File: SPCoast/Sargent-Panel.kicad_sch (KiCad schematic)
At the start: 9 parts, among them U1 0x2C

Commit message: refactor(kicad): Name on every device, office unit and encoding; Kind on the JMRI drivers; Driver-JMRI-Light
The owner's rulings of 2026-10-24 on the review of ADR 0008 rev 4: Name = ${Value}
is the identity key everywhere, devices included; the OfficeUnit's Columns is
derived and struck; a JMRI driver carries no address and is keyed by its object
class and the device it serves, the class carried by Kind (TURNOUT, SENSOR,
SIGNALMAST, LIGHT); Driver-JMRI-Light (ADR 0005 §8: ON, INTENSITY) for a lamp
JMRI drives, and the two Gilroy Interchange maintainer-call lamps MC1 and MC2
become Lights (they were Sensors, which JMRI only displays).

Script: SPCoast/edits/2026-10-24-names-kind-light.py. Libraries: Name on 36
symbols (OfficeUnit, 5 encodings, 12 PANEL, 18 DEVICE), Columns off OfficeUnit,
Kind on 5 JMRI drivers, Driver-JMRI-Light added (the Sensor's pin positions,
INTENSITY as pin 3 below, no-connect on the two placed instances). Sheets: 359
Name instance fields, 16 Kind, 2 lib_id swaps, caches refreshed (no pin moved on
a refreshed symbol).

Verified: gate --check production/SPCoast.net production/names-after.net PASS:
same parts, same connectivity, Name == Value on all 273 named instances (47
heads with Value "~" resolve to an empty Name), Columns dropped once, Kind on 16
drivers, 2 Sensor -> Light with pin 1 reading ON; ERC 0 before and after.
Subdivision lint_symbol_fields: 99 symbols, 0 errors (Kind now allowed on
IODRIVER). production/SPCoast.net is the new export (production/ is untracked).

Co-Authored-By: Claude Fable 5.1 <noreply@anthropic.com>
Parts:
- CDE1, LKL1, LMP1, LMP2, LMP3, MCK1, MCL1: Name (none) -> ${Value}
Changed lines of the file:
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@@
+			)
+		)
+		(property "Name" "${Value}"
+			(at 80.01 104.14 0)
+			(hide yes)
+			(show_name no)
+			(do_not_autoplace no)
+			(effects
+				(font
+					(size 1.27 1.27)
+				)
 			)
 		)
@@
 			)
 		)
+		(property "Name" "${Value}"
+			(at 80.01 36.83 0)
+			(hide yes)
+			(show_name no)
+			(do_not_autoplace no)
+			(effects
+				(font
+					(size 1.27 1.27)
+				)
+			)
+		)
 		(property "Appliance" "lamp"
 			(at 80.01 39.37 0)
@@
 			)
 		)
+		(property "Name" "${Value}"
+			(at 80.01 31.75 0)
+			(hide yes)
+			(show_name no)
+			(do_not_autoplace no)
+			(effects
+				(font
+					(size 1.27 1.27)
+				)
+			)
+		)
 		(property "Appliance" "lamp"
 			(at 80.01 34.29 0)
@@
 			)
 		)
+		(property "Name" "${Value}"
+			(at 80.01 63.5 0)
+			(hide yes)
+			(show_name no)
+			(do_not_autoplace no)
+			(effects
+				(font
+					(size 1.27 1.27)
+				)
+			)
+		)
 		(property "Appliance" "lever"
 			(at 80.645 74.93 0)
@@
 			)
 		)
+		(property "Name" "${Value}"
+			(at 80.01 97.79 0)
+			(hide yes)
+			(show_name no)
+			(do_not_autoplace no)
+			(effects
+				(font
+					(size 1.27 1.27)
+				)
+			)
+		)
 		(property "Appliance" "lever"
 			(at 80.01 90.17 0)
@@
 			)
 		)
+		(property "Name" "${Value}"
+			(at 80.01 48.26 0)
+			(hide yes)
+			(show_name no)
+			(do_not_autoplace no)
+			(effects
+				(font
+					(size 1.27 1.27)
+				)
+			)
+		)
 		(property "Appliance" "lever"
 			(at 86.36 44.45 0)
@@
 			)
 		)
+		(property "Name" "${Value}"
+			(at 80.01 26.67 0)
+			(hide yes)
+			(show_name no)
+			(do_not_autoplace no)
+			(effects
+				(font
+					(size 1.27 1.27)
+				)
+			)
+		)
 		(property "Appliance" "lamp"
 			(at 80.01 29.21 0)
@@
 			(hide yes)
 			(show_name no)
+			(do_not_autoplace no)
+			(effects
+				(font
+					(size 1.27 1.27)
+				)
+			)
+		)
+		(property "Name" "${Value}"
+			(at 80.01 63.5 0)
+			(hide yes)
+			(show_name no)

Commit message: feat(spcoast): every desk column names its CP Name
The owner's edit in KiCad: each PanelColumn carries a CP Name. On an
AAR codeline it may name the interlocking (Christopher, Gilroy
Interchange); on the 506 it names the house.

Verified: a fresh kicad-cli netlist compiles with no column.cp_name
diagnostics; the three column.house errors (columns 3, 4, 9) are
resolved by the importer rule, not the drawing.

Co-Authored-By: Claude Opus 5.5 <noreply@anthropic.com>
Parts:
- COL1: CP Name (none) -> Sargent
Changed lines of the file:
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@@
 			)
 		)
-		(property "CP Name" ""
+		(property "CP Name" "Sargent"
 			(at 80.645 132.08 0)
 			(show_name yes)

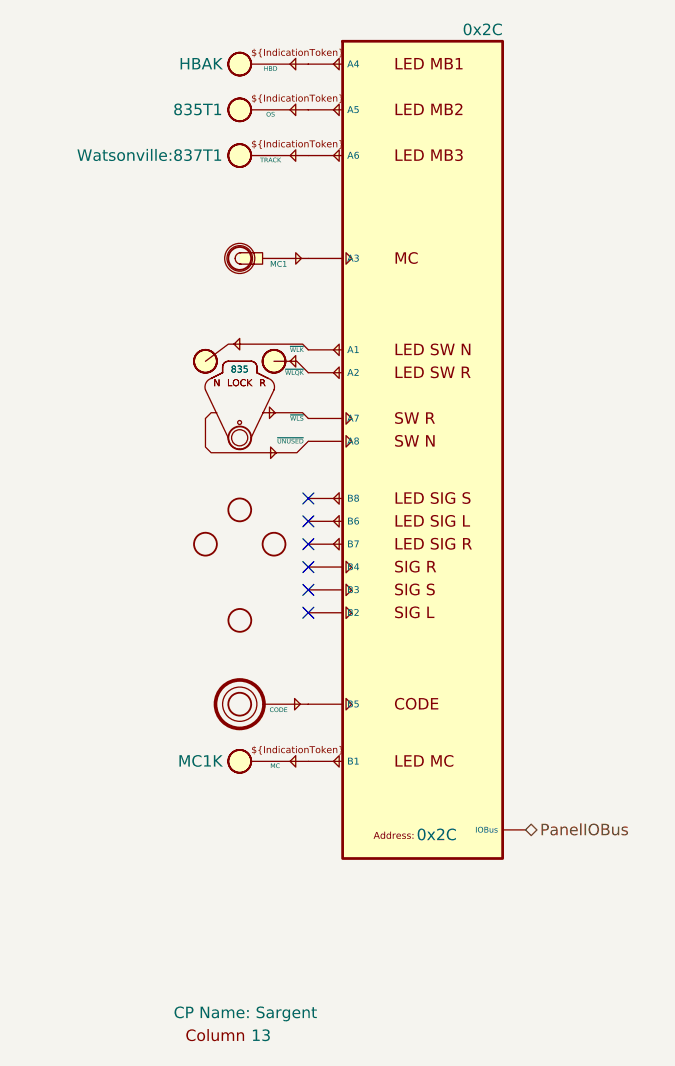
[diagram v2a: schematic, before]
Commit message: feat(spcoast): per-pin token fields on the panels, lamp Indication expressions, maintainer calls named 1MC
Applies the symbol rulings of 2026-10-28 to every sheet: the lib_symbols
caches of the changed symbols are the library's copies (this also clears
the stale PanelMCall and MaintainerCall caches), and every placed
instance gets the new hidden Control.*/Indication.* fields, loses
PanelLock Invert, and PanelMCall's whole-symbol Control and Indication
(Pin.MCK binary). Model lamps' IndicationToken becomes Indication: each
comma-separated circuit gets its K, qualifiers kept, joined with " | "
(795T1,01T,799T1 -> 795T1K | 01TK | 799T1K).

Maintainer calls in Christopher (1, 2), Corporal, Luchessa and Sargent
follow Gilroy Interchange (5dad54f): Value MC<n> -> <n>, Name ${Value}MC,
and the separate PanelMCall-Lamp is replaced by unit 2 of the same
PanelMCall at the old lamp's position, so its MCK pin sits where the
LAMP pin was. The old lamps' Column pin touched PanelColumn pin 8
directly (no wire); that pin is now unconnected, as on Gilroy
Interchange. Gilroy Interchange's local MaintainerCall_1 cache and its
two trackplan calls lose Indication.

Verified: fresh netlist before/after: components 752 -> 747 (the five
lamps), nets 1028 -> 1028; each old LAMP-pin net now holds the lever's
unit-2 MCK pin (pin 3) on the same expander pin (B1, pin 9); the levers'
nets are renamed only (~{S} -> ~{MCS}, unit suffix A); no other net
changed. Every field difference is an intended one. ERC 18 -> 1
violations (lib_symbol_mismatch 17 -> 0; pre-existing Sargent AUX1
pin_not_connected remains).

Co-Authored-By: Claude Opus 5.5 <noreply@anthropic.com>
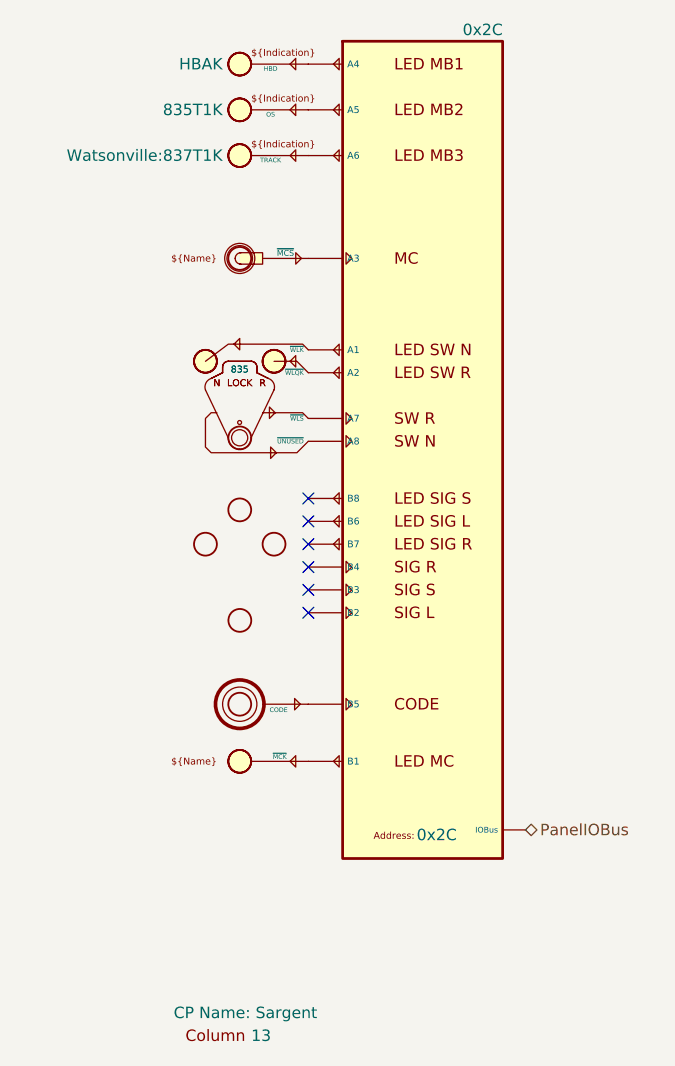
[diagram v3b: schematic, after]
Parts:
- removed MCK1: MC, symbol Railroad-Office:PanelMCall-Lamp
- added unit 2 of MCL1
- LKL1: Control.WLS (none) -> ${Value}WLS; Indication.WLK (none) -> !${Value}WLK; Indication.WLQK (none) -> ${Value}WLQK; Invert WLK -> (none)
- LMP1: Indication (none) -> HBAK; IndicationToken HBAK -> (none)
- LMP2: Indication (none) -> 835T1K; IndicationToken 835T1 -> (none)
- LMP3: Indication (none) -> Watsonville:837T1K; IndicationToken Watsonville:837T1 -> (none)
- MCL1: value MC1 -> 1; Control.MCS (none) -> ${Value}MCS; Indication.MCK (none) -> ${Value}MCK; Name ${Value} -> ${Value}MC; Pin.MCK (none) -> binary; Pin.MCS (none) -> binary; Pin.S binary -> (none)
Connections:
- net at U1.9 (B1): now also MCL1.3 (~{MCK})
